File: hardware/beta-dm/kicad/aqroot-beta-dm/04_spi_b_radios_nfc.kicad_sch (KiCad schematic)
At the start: 22 parts, among them U7 E07-400M10S, U8 E22-900M22S, U9 ST25R3916-AQET

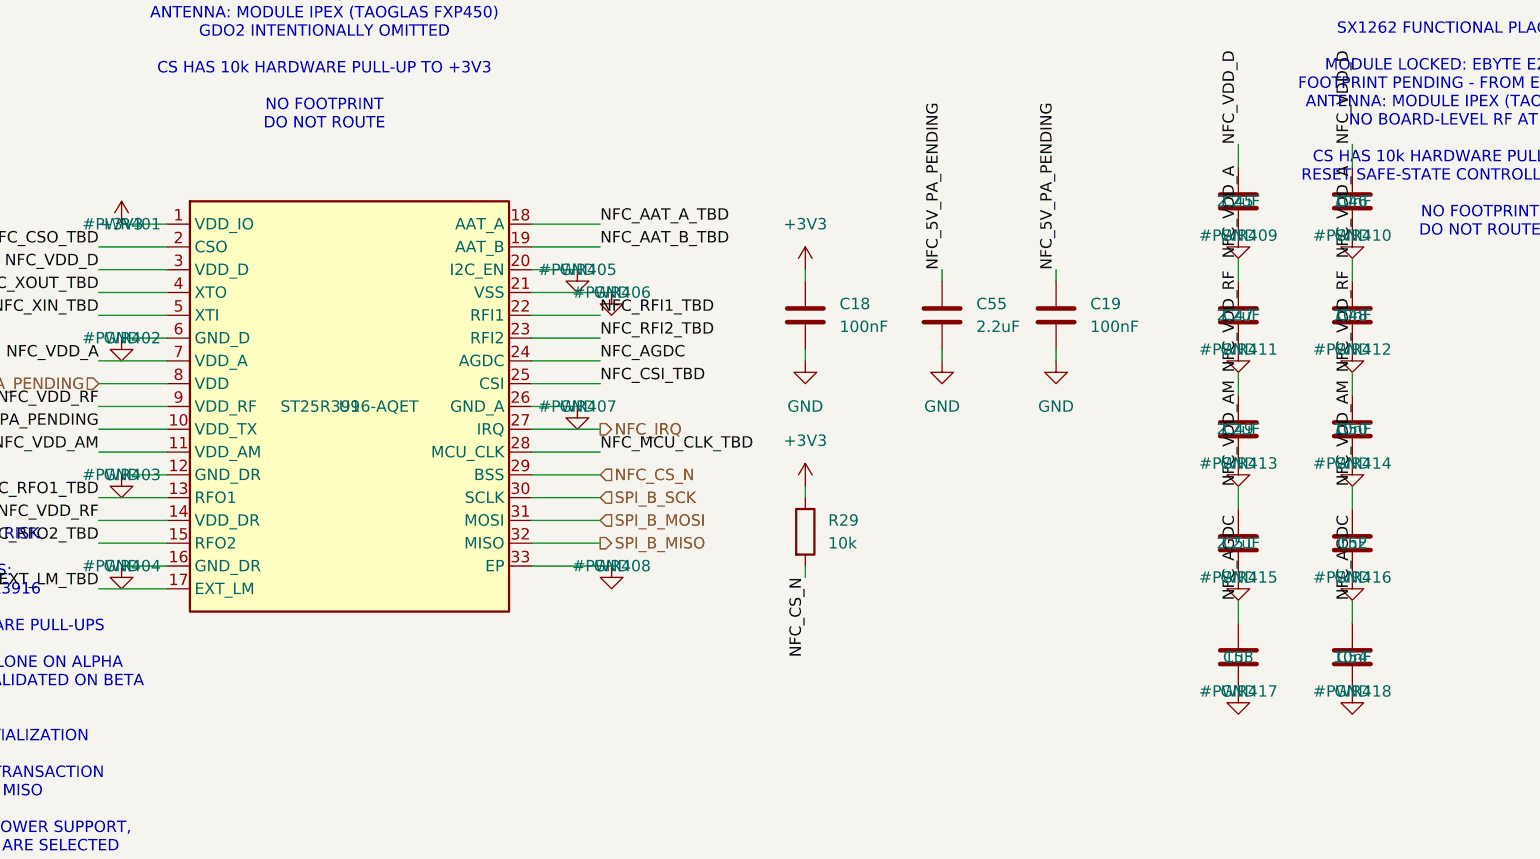
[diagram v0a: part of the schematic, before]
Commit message: hardware(beta-dm): DNP becomes manufacturing data, not a markdown list
Marks the CTO-approved Beta-DM DNP set in KiCad's native convention and
generates the factory-facing package from it. No copper changes.

29 references gain (dnp yes) in the schematic and the matching `dnp` footprint
attribute on the PCB - the same convention the design already used for its five
pre-existing DNP parts C21, C22, R68, R49, R50, which is why nothing new was
invented here:

  NFC front end   U9 C45 C46 C47 C48 C49 C50 C51 C52 C53 C54
  NFC 5 V boost   U13 L2 R44 R45 C34 C35 C19 C55
  speaker         U5 J6
  IR transmitter  D1 Q1 R22 R23 R24
  IR receiver     U6 R21 C11

in_bom is deliberately left ON. A DNP part must still appear in the BOM flagged
DNP so the factory sees it and sees not to fit it; hiding it invites someone to
"helpfully" add it back. in_pos_files is left alone too - the position file is
generated with --exclude-dnp instead, which matches how the five pre-existing
DNP parts are already handled.

Generated into hardware/beta-dm/fab/:

  aqroot-Beta-DM-BOM-fitted.csv        parts to buy and place, DNP excluded
  aqroot-Beta-DM-BOM-full.csv          every part with a DNP column
  aqroot-Beta-DM-DO-NOT-POPULATE.csv   34 refs, each with its reason
  aqroot-Beta-DM-pos-fitted.csv        pick-and-place, DNP excluded
  aqroot-Beta-DM-pos-all.csv           reference only, do not feed the machine
  aqroot-Beta-DM-assembly-{top,bottom}.pdf   DNP parts crossed out
  ASSEMBLY-DNP-CONTROL.md              the control document

Verified: the fitted position file contains 139 of 173 footprints and none of
the 34 DNP refs; U9, U13, U5, J6, D1, Q1 and U6 are all absent from it. The
assembly PDFs cross out DNP automatically because the project already carries
crossoutdnponfab and sketchdnponfab.

Electrical audit of the ASSEMBLED circuit, not the artwork. No fitted IC pin is
left on a net with neither a driver nor a passive. SPI-B loses only U9's three
pins and keeps U1, U7 and U8, whic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
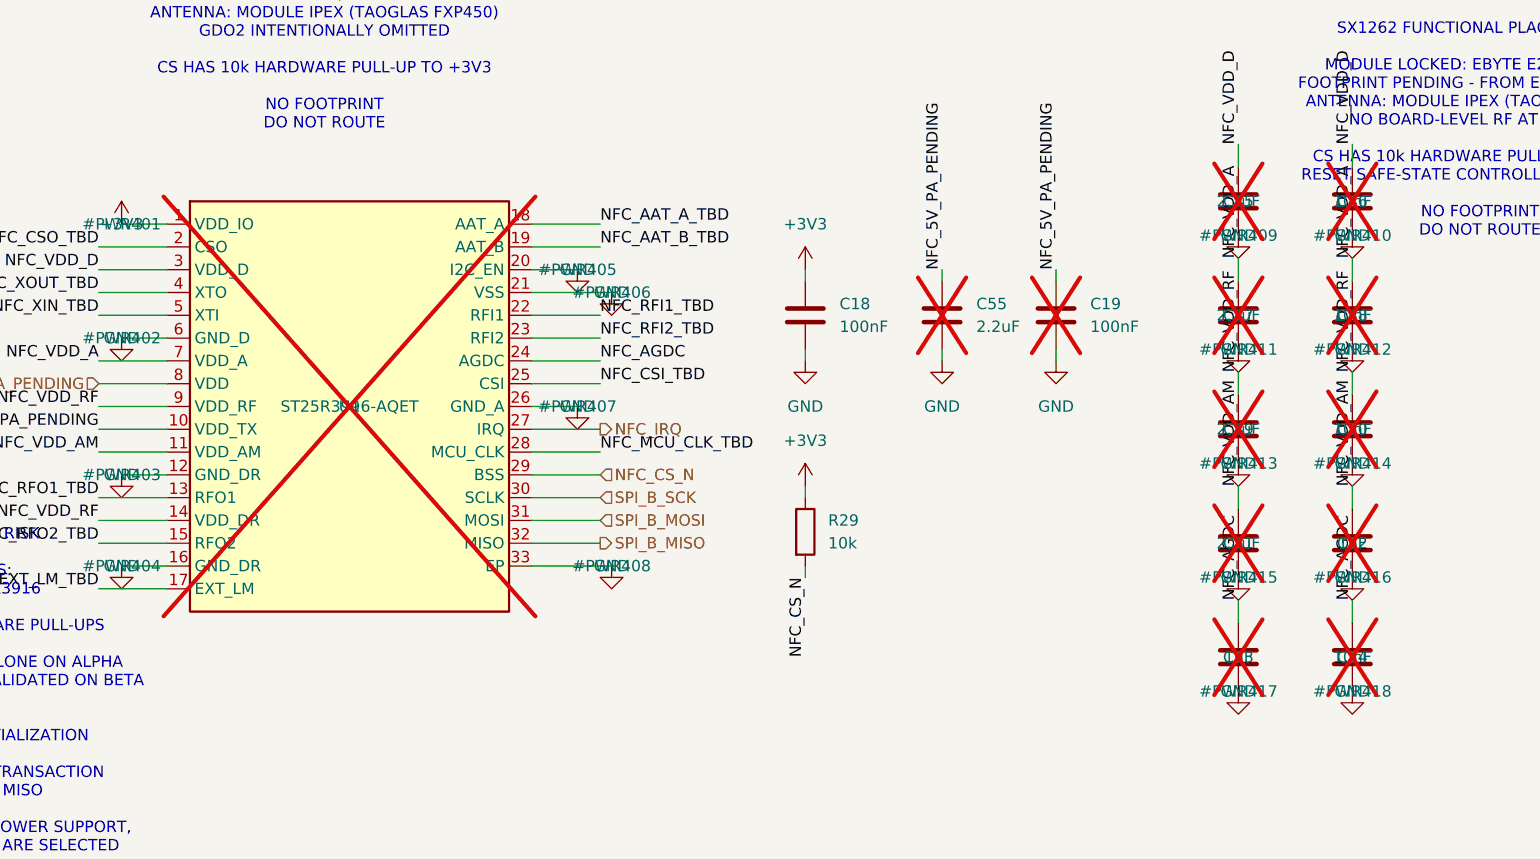
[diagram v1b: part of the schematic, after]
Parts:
- C19, C45, C46, C47, C48, C49, C50, C51, C52, C53, C54, C55, U9: now not fitted
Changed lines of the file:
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@@
 		(on_board yes)
 		(in_pos_files yes)
-		(dnp no)
+		(dnp yes)
 		(fields_autoplaced yes)
 		(property "Reference" "C19"
@@
 		(in_bom yes)
 		(on_board yes)
-		(dnp no)
+		(dnp yes)
 		(fields_autoplaced yes)
 		(property "Reference" "U9"
@@
 		(in_bom yes)
 		(on_board yes)
-		(dnp no)
+		(dnp yes)
 		(fields_autoplaced yes)
 		(property "Reference" "C45"
@@
 		(in_bom yes)
 		(on_board yes)
-		(dnp no)
+		(dnp yes)
 		(fields_autoplaced yes)
 		(property "Reference" "C46"
@@
 		(in_bom yes)
 		(on_board yes)
-		(dnp no)
+		(dnp yes)
 		(fields_autoplaced yes)
 		(property "Reference" "C47"
@@
 		(in_bom yes)
 		(on_board yes)
-		(dnp no)
+		(dnp yes)
 		(fields_autoplaced yes)
 		(property "Reference" "C48"
@@
 		(in_bom yes)
 		(on_board yes)
-		(dnp no)
+		(dnp yes)
 		(fields_autoplaced yes)
 		(property "Reference" "C49"
@@
 		(in_bom yes)
 		(on_board yes)
-		(dnp no)
+		(dnp yes)
 		(fields_autoplaced yes)
 		(property "Reference" "C50"
@@
 		(in_bom yes)
 		(on_board yes)
-		(dnp no)
+		(dnp yes)
 		(fields_autoplaced yes)
 		(property "Reference" "C51"
@@
 		(in_bom yes)
 		(on_board yes)
-		(dnp no)
+		(dnp yes)
 		(fields_autoplaced yes)
 		(property "Reference" "C52"
@@
 		(in_bom yes)
 		(on_board yes)
-		(dnp no)
+		(dnp yes)
 		(fields_autoplaced yes)
 		(property "Reference" "C53"
@@
 		(in_bom yes)
 		(on_board yes)
-		(dnp no)
+		(dnp yes)
 		(fields_autoplaced yes)
 		(property "Reference" "C54"
@@
 		(on_board yes)
 		(in_pos_files yes)
-		(dnp no)
+		(dnp yes)
 		(fields_autoplaced yes)
 		(property "Reference" "C55"
